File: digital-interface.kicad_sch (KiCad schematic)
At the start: 37 parts, among them U301 Si8641BD-B-IS2, U302 R05C05TE05S

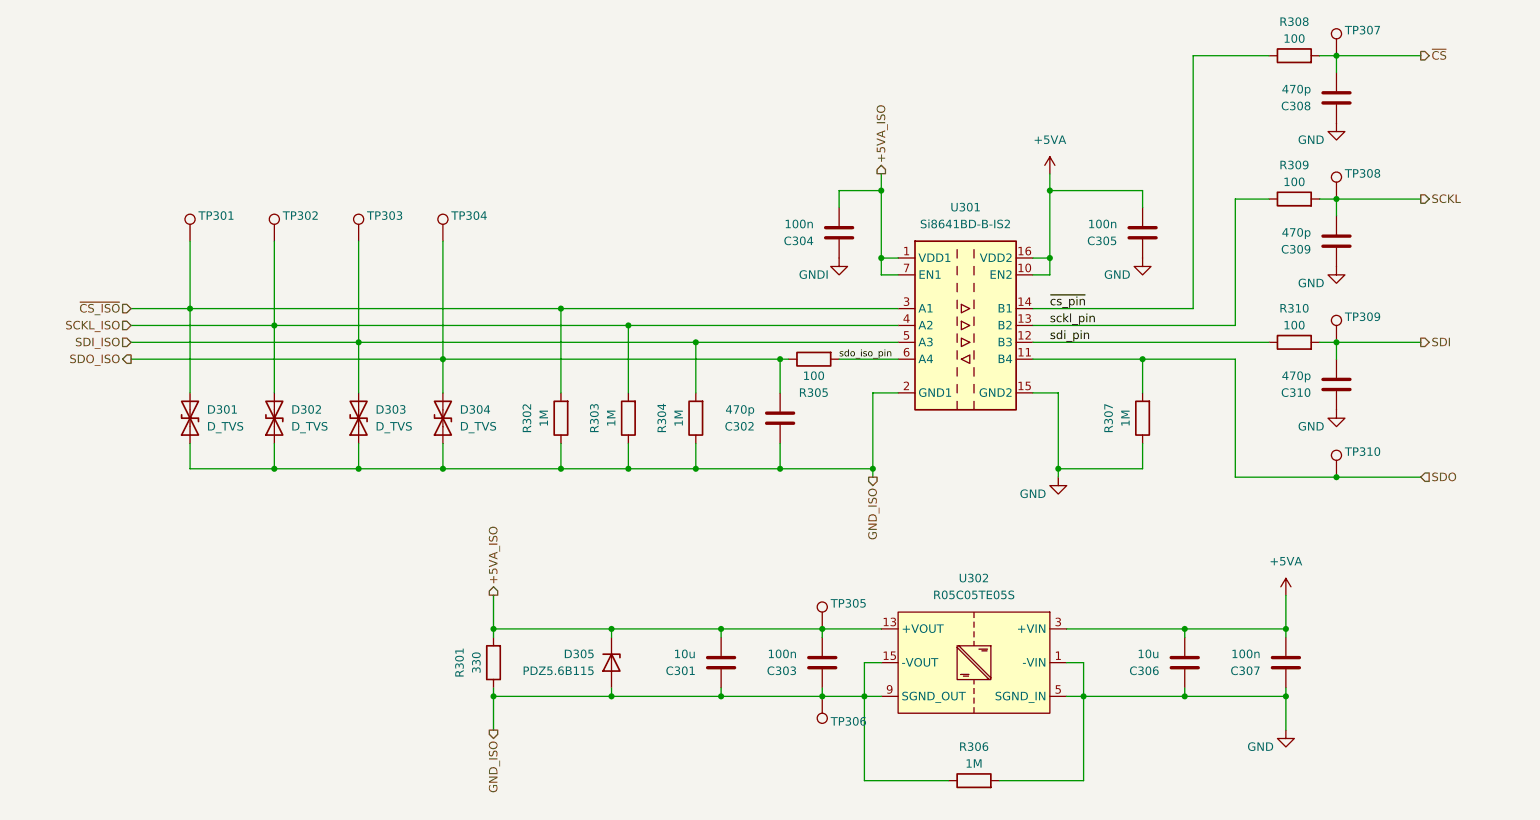
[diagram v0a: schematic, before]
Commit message: fix digital-interface schematic connections
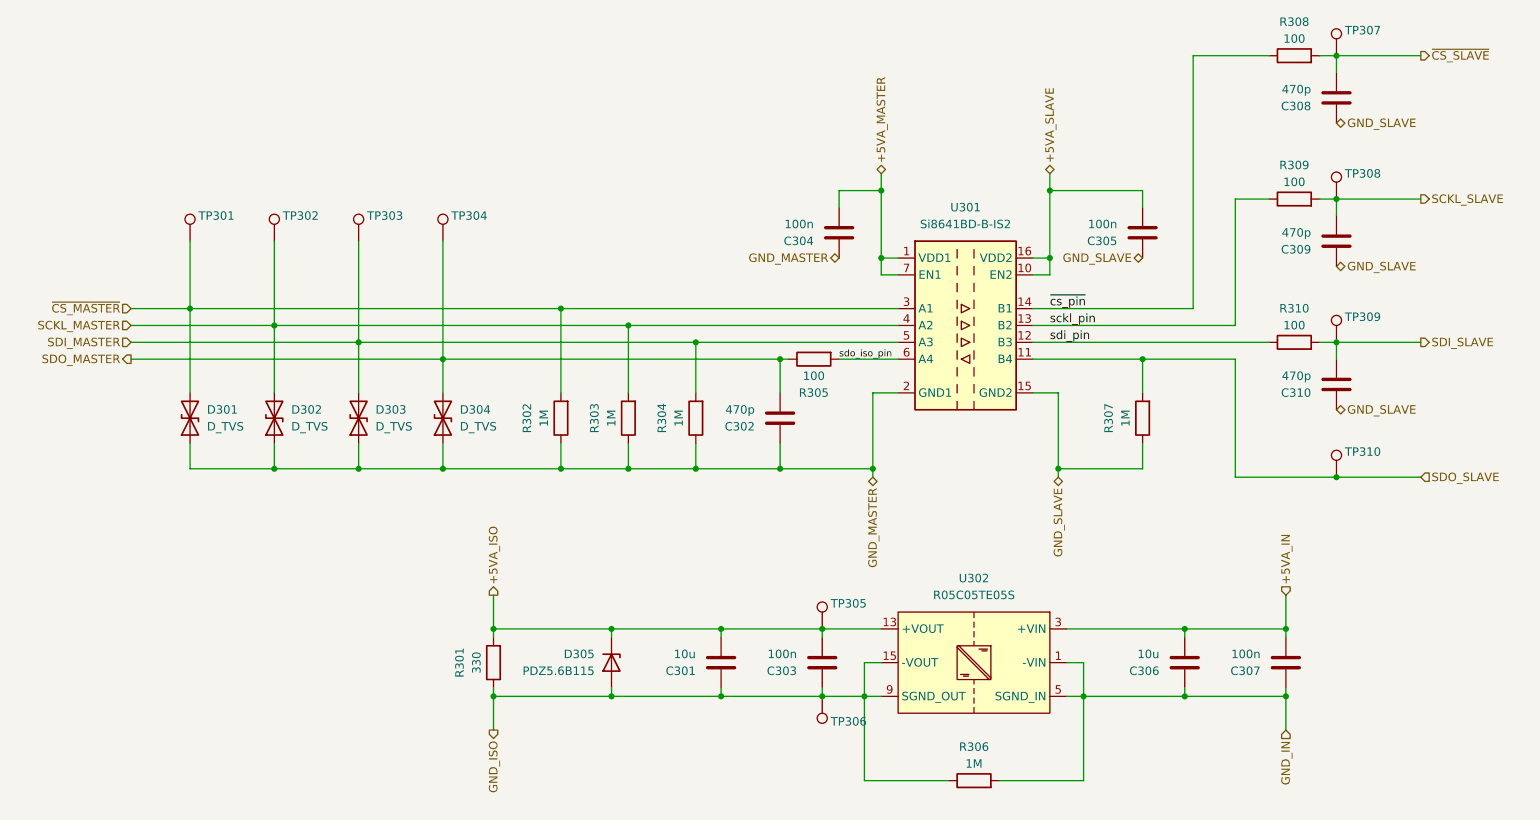
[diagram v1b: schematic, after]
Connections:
- net +5VA_ISO: no longer C304.2, U301.1 (VDD1), U301.7 (EN1)
- net GND_ISO: no longer C302.1, D301.1 (A1), D302.1 (A1), D303.1 (A1), D304.1 (A1), R302.1, R303.1, R304.1, U301.2 (GND1), U301.8 (GND1)
- net +5VA renamed +5VA_IN
- net +5VA_IN: no longer C305.2, U301.10 (EN2), U301.16 (VDD2)
- net GND renamed GND_IN
- net GND_IN: no longer C305.1, C308.1, C309.1, C310.1, R307.1, U301.15 (GND2), U301.9 (GND2)
- net GNDI renamed GND_MASTER
- net GND_MASTER: now also C302.1, D301.1 (A1), D302.1 (A1), D303.1 (A1), D304.1 (A1), R302.1, R303.1, R304.1, U301.2 (GND1), U301.8 (GND1)
- net SCKL renamed SCKL_SLAVE
- net SCKL_ISO renamed SCKL_MASTER
- net SDI renamed SDI_SLAVE
- net SDI_ISO renamed SDI_MASTER
- net SDO renamed SDO_SLAVE
- net SDO_ISO renamed SDO_MASTER
- net ~{CS_ISO} renamed ~{CS_MASTER}
- net ~{CS} renamed ~{CS_SLAVE}
- new net +5VA_MASTER: C304.2, U301.1 (VDD1), U301.7 (EN1)
- new net +5VA_SLAVE: C305.2, U301.10 (EN2), U301.16 (VDD2)
- new net GND_SLAVE: C305.1, C308.1, C309.1, C310.1, R307.1, U301.15 (GND2), U301.9 (GND2)

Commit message: add export of symbol libray, edit symbol links
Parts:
- C301, C302, C303, C304, C305, C306, C307, C308, C309, C310: symbol enclosure:C -> meas:C
- D301, D302, D303, D304: symbol enclosure:D_TVS -> meas:D_TVS
- D305: symbol enclosure:D_Zener -> meas:D_Zener
- R301, R302, R303, R304, R305, R306, R307, R308, R309, R310: symbol enclosure:R -> meas:R
- TP301, TP302, TP303, TP304, TP305, TP306, TP307, TP308, TP309, TP310: symbol enclosure:TestPoint -> meas:TestPoint
- U301: symbol enclosure:Si8641BD-B-IS2 -> meas:Si8641BD-B-IS2
- U302: symbol enclosure:R05C05TE05S -> meas:R05C05TE05S
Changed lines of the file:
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@@
 	)
 	(symbol
-		(lib_id "enclosure:D_TVS")
+		(lib_id "meas:D_TVS")
 		(at 49.53 85.09 90)
 		(unit 1)
@@
 	)
 	(symbol
-		(lib_id "enclosure:D_TVS")
+		(lib_id "meas:D_TVS")
 		(at 62.23 85.09 90)
 		(unit 1)
@@
 	)
 	(symbol
-		(lib_id "enclosure:C")
+		(lib_id "meas:C")
 		(at 222.25 36.83 180)
 		(unit 1)
@@
 	)
 	(symbol
-		(lib_id "enclosure:C")
+		(lib_id "meas:C")
 		(at 214.63 121.92 180)
 		(unit 1)
@@
 	)
 	(symbol
-		(lib_id "enclosure:TestPoint")
+		(lib_id "meas:TestPoint")
 		(at 74.93 58.42 0)
 		(unit 1)
@@
 	)
 	(symbol
-		(lib_id "enclosure:TestPoint")
+		(lib_id "meas:TestPoint")
 		(at 222.25 52.07 0)
 		(unit 1)
@@
 	)
 	(symbol
-		(lib_id "enclosure:C")
+		(lib_id "meas:C")
 		(at 193.04 57.15 180)
 		(unit 1)
@@
 	)
 	(symbol
-		(lib_id "enclosure:TestPoint")
+		(lib_id "meas:TestPoint")
 		(at 49.53 58.42 0)
 		(unit 1)
@@
 	)
 	(symbol
-		(lib_id "enclosure:R")
+		(lib_id "meas:R")
 		(at 143.51 76.2 90)
 		(mirror x)
@@
 	)
 	(symbol
-		(lib_id "enclosure:C")
+		(lib_id "meas:C")
 		(at 199.39 121.92 180)
 		(unit 1)
@@
 	)
 	(symbol
-		(lib_id "enclosure:R")
+		(lib_id "meas:R")
 		(at 167.64 139.7 90)
 		(unit 1)
@@
 	)
 	(symbol
-		(lib_id "enclosure:TestPoint")
+		(lib_id "meas:TestPoint")
 		(at 222.25 93.98 0)
 		(unit 1)
@@
 	)
 	(symbol
-		(lib_id "enclosure:R")
+		(lib_id "meas:R")
 		(at 125.73 85.09 180)
 		(unit 1)
@@
 	)
 	(symbol
-		(lib_id "enclosure:R")
+		(lib_id "meas:R")
 		(at 215.9 30.48 90)
 		(unit 1)
@@
 	)
 	(symbol
-		(lib_id "enclosure:D_Zener")
+		(lib_id "meas:D_Zener")
 		(at 113.03 121.92 270)
 		(unit 1)
@@
 	)
 	(symbol
-		(lib_id "enclosure:C")
+		(lib_id "meas:C")
 		(at 222.25 80.01 180)
 		(unit 1)
@@
 	)
 	(symbol
-		(lib_id "enclosure:R")
+		(lib_id "meas:R")
 		(at 95.25 121.92 180)
 		(unit 1)
@@
 	)
 	(symbol
-		(lib_id "enclosure:TestPoint")
+		(lib_id "meas:TestPoint")
 		(at 87.63 58.42 0)
 		(unit 1)
@@
 	)
 	(symbol
-		(lib_id "enclosure:C")
+		(lib_id "meas:C")
 		(at 222.25 58.42 180)
 		(unit 1)
@@
 	)
 	(symbol
-		(lib_id "enclosure:C")
+		(lib_id "meas:C")
 		(at 129.54 121.92 180)
 		(unit 1)
@@
 	)
 	(symbol
-		(lib_id "enclosure:D_TVS")
+		(lib_id "meas:D_TVS")
 		(at 74.93 85.09 90)
 		(unit 1)
@@
 	)
 	(symbol
-		(lib_id "enclosure:R")
+		(lib_id "meas:R")
 		(at 215.9 52.07 90)
 		(unit 1)
@@
 	)
 	(symbol
-		(lib_id "enclosure:TestPoint")
+		(lib_id "meas:TestPoint")
 		(at 222.25 73.66 0)
 		(unit 1)
@@
 	)
 	(symbol
-		(lib_id "enclosure:R05C05TE05S")
+		(lib_id "meas:R05C05TE05S")
 		(at 167.64 121.92 0)
 		(mirror y)
@@
 	)
 	(symbol
-		(lib_id "enclosure:R")
+		(lib_id "meas:R")
 		(at 215.9 73.66 90)
 		(unit 1)
@@
 	)
 	(symbol
-		(lib_id "enclosure:TestPoint")
+		(lib_id "meas:TestPoint")
 		(at 144.78 116.84 0)
 		(unit 1)
@@
 	)
 	(symbol
-		(lib_id "enclosure:TestPoint")
+		(lib_id "meas:TestPoint")
 		(at 62.23 58.42 0)
 		(unit 1)
@@
 	)
 	(symbol
-		(lib_id "enclosure:C")
+		(lib_id "meas:C")
 		(at 144.78 121.92 180)
 		(unit 1)
@@
 	)
 	(symbol
-		(lib_id "enclosure:TestPoint")
+		(lib_id "meas:TestPoint")
 		(at 222.25 30.48 0)
 		(unit 1)
@@
 	)
 	(symbol
-		(lib_id "enclosure:TestPoint")
+		(lib_id "meas:TestPoint")
 		(at 144.78 127 0)
 		(mirror x)
@@
 	)
 	(symbol
-		(lib_id "enclosure:R")
+		(lib_id "meas:R")
 		(at 105.41 85.09 180)
 		(unit 1)
@@
 	)
 	(symbol
-		(lib_id "enclosure:R")
+		(lib_id "meas:R")
 		(at 115.57 85.09 180)
 		(unit 1)
@@
 	)
 	(symbol
-		(lib_id "enclosure:D_TVS")
+		(lib_id "meas:D_TVS")
 		(at 87.63 85.09 90)
 		(unit 1)
@@
 	)
 	(symbol
-		(lib_id "enclosure:C")
+		(lib_id "meas:C")
 		(at 138.43 85.09 180)
 		(unit 1)
@@
 	)
 	(symbol
-		(lib_id "enclosure:Si8641BD-B-IS2")
+		(lib_id "meas:Si8641BD-B-IS2")
 		(at 166.37 71.12 0)
 		(unit 1)
@@
 	)
 	(symbol
-		(lib_id "enclosure:R")
+		(lib_id "meas:R")
 		(at 193.04 85.09 180)
 		(unit 1)
@@
 	)
 	(symbol
-		(lib_id "enclosure:C")
+		(lib_id "meas:C")
 		(at 147.32 57.15 180)
 		(unit 1)

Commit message: add export of footprint library, edit footprint links
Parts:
- C301, C306: footprint enclosure:C_1210_3225Metric_Pad1.33x2.70mm_HandSolder -> meas:C_1210_3225Metric_Pad1.33x2.70mm_HandSolder
- C302, C303, C304, C305, C307, C308, C309, C310: footprint enclosure:C_0805_2012Metric_Pad1.18x1.45mm_HandSolder -> meas:C_0805_2012Metric_Pad1.18x1.45mm_HandSolder
- D301, D302, D303, D304, D305: footprint enclosure:D_SOD-323_HandSoldering -> meas:D_SOD-323_HandSoldering
- R301, R302, R303, R304, R305, R306, R307, R308, R309, R310: footprint enclosure:R_1210_3225Metric_Pad1.30x2.65mm_HandSolder -> meas:R_1210_3225Metric_Pad1.30x2.65mm_HandSolder
- TP301, TP302, TP303, TP304, TP305, TP306, TP307, TP308, TP309, TP310: footprint enclosure:TP_0805_2012Metric -> meas:TP_0805_2012Metric
- U301, U302: footprint enclosure:SOIC-16W_7.5x10.3mm_P1.27mm -> meas:SOIC-16W_7.5x10.3mm_P1.27mm
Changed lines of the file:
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@@
 			)
 		)
-		(property "Footprint" "enclosure:D_SOD-323_HandSoldering"
+		(property "Footprint" "meas:D_SOD-323_HandSoldering"
 			(at 49.53 85.09 0)
 			(effects
@@
 			)
 		)
-		(property "Footprint" "enclosure:D_SOD-323_HandSoldering"
+		(property "Footprint" "meas:D_SOD-323_HandSoldering"
 			(at 62.23 85.09 0)
 			(effects
@@
 			)
 		)
-		(property "Footprint" "enclosure:C_0805_2012Metric_Pad1.18x1.45mm_HandSolder"
+		(property "Footprint" "meas:C_0805_2012Metric_Pad1.18x1.45mm_HandSolder"
 			(at 221.2848 33.02 0)
 			(effects
@@
 			)
 		)
-		(property "Footprint" "enclosure:C_0805_2012Metric_Pad1.18x1.45mm_HandSolder"
+		(property "Footprint" "meas:C_0805_2012Metric_Pad1.18x1.45mm_HandSolder"
 			(at 213.6648 118.11 0)
 			(effects
@@
 			)
 		)
-		(property "Footprint" "enclosure:TP_0805_2012Metric"
+		(property "Footprint" "meas:TP_0805_2012Metric"
 			(at 80.01 58.42 0)
 			(effects
@@
 			)
 		)
-		(property "Footprint" "enclosure:TP_0805_2012Metric"
+		(property "Footprint" "meas:TP_0805_2012Metric"
 			(at 227.33 52.07 0)
 			(effects
@@
 			)
 		)
-		(property "Footprint" "enclosure:C_0805_2012Metric_Pad1.18x1.45mm_HandSolder"
+		(property "Footprint" "meas:C_0805_2012Metric_Pad1.18x1.45mm_HandSolder"
 			(at 192.0748 53.34 0)
 			(effects
@@
 			)
 		)
-		(property "Footprint" "enclosure:TP_0805_2012Metric"
+		(property "Footprint" "meas:TP_0805_2012Metric"
 			(at 54.61 58.42 0)
 			(effects
@@
 			)
 		)
-		(property "Footprint" "enclosure:R_1210_3225Metric_Pad1.30x2.65mm_HandSolder"
+		(property "Footprint" "meas:R_1210_3225Metric_Pad1.30x2.65mm_HandSolder"
 			(at 143.51 74.422 90)
 			(effects
@@
 			)
 		)
-		(property "Footprint" "enclosure:C_1210_3225Metric_Pad1.33x2.70mm_HandSolder"
+		(property "Footprint" "meas:C_1210_3225Metric_Pad1.33x2.70mm_HandSolder"
 			(at 198.4248 118.11 0)
 			(effects
@@
 			)
 		)
-		(property "Footprint" "enclosure:R_1210_3225Metric_Pad1.30x2.65mm_HandSolder"
+		(property "Footprint" "meas:R_1210_3225Metric_Pad1.30x2.65mm_HandSolder"
 			(at 167.64 141.478 90)
 			(effects
@@
 			)
 		)
-		(property "Footprint" "enclosure:TP_0805_2012Metric"
+		(property "Footprint" "meas:TP_0805_2012Metric"
 			(at 227.33 93.98 0)
 			(effects
@@
 			)
 		)
-		(property "Footprint" "enclosure:R_1210_3225Metric_Pad1.30x2.65mm_HandSolder"
+		(property "Footprint" "meas:R_1210_3225Metric_Pad1.30x2.65mm_HandSolder"
 			(at 127.508 85.09 90)
 			(effects
@@
 			)
 		)
-		(property "Footprint" "enclosure:R_1210_3225Metric_Pad1.30x2.65mm_HandSolder"
+		(property "Footprint" "meas:R_1210_3225Metric_Pad1.30x2.65mm_HandSolder"
 			(at 215.9 32.258 90)
 			(effects
@@
 			)
 		)
-		(property "Footprint" "enclosure:D_SOD-323_HandSoldering"
+		(property "Footprint" "meas:D_SOD-323_HandSoldering"
 			(at 113.03 121.92 0)
 			(effects
@@
 			)
 		)
-		(property "Footprint" "enclosure:C_0805_2012Metric_Pad1.18x1.45mm_HandSolder"
+		(property "Footprint" "meas:C_0805_2012Metric_Pad1.18x1.45mm_HandSolder"
 			(at 221.2848 76.2 0)
 			(effects
@@
 			)
 		)
-		(property "Footprint" "enclosure:R_1210_3225Metric_Pad1.30x2.65mm_HandSolder"
+		(property "Footprint" "meas:R_1210_3225Metric_Pad1.30x2.65mm_HandSolder"
 			(at 97.028 121.92 90)
 			(effects
@@
 			)
 		)
-		(property "Footprint" "enclosure:TP_0805_2012Metric"
+		(property "Footprint" "meas:TP_0805_2012Metric"
 			(at 92.71 58.42 0)
 			(effects
@@
 			)
 		)
-		(property "Footprint" "enclosure:C_0805_2012Metric_Pad1.18x1.45mm_HandSolder"
+		(property "Footprint" "meas:C_0805_2012Metric_Pad1.18x1.45mm_HandSolder"
 			(at 221.2848 54.61 0)
 			(effects
@@
 			)
 		)
-		(property "Footprint" "enclosure:C_1210_3225Metric_Pad1.33x2.70mm_HandSolder"
+		(property "Footprint" "meas:C_1210_3225Metric_Pad1.33x2.70mm_HandSolder"
 			(at 128.5748 118.11 0)
 			(effects
@@
 			)
 		)
-		(property "Footprint" "enclosure:D_SOD-323_HandSoldering"
+		(property "Footprint" "meas:D_SOD-323_HandSoldering"
 			(at 74.93 85.09 0)
 			(effects
@@
 			)
 		)
-		(property "Footprint" "enclosure:R_1210_3225Metric_Pad1.30x2.65mm_HandSolder"
+		(property "Footprint" "meas:R_1210_3225Metric_Pad1.30x2.65mm_HandSolder"
 			(at 215.9 53.848 90)
 			(effects
@@
 			)
 		)
-		(property "Footprint" "enclosure:TP_0805_2012Metric"
+		(property "Footprint" "meas:TP_0805_2012Metric"
 			(at 227.33 73.66 0)
 			(effects
@@
 			)
 		)
-		(property "Footprint" "enclosure:SOIC-16W_7.5x10.3mm_P1.27mm"
+		(property "Footprint" "meas:SOIC-16W_7.5x10.3mm_P1.27mm"
 			(at 167.64 121.92 0)
 			(effects
@@
 			)
 		)
-		(property "Footprint" "enclosure:R_1210_3225Metric_Pad1.30x2.65mm_HandSolder"
+		(property "Footprint" "meas:R_1210_3225Metric_Pad1.30x2.65mm_HandSolder"
 			(at 215.9 75.438 90)
 			(effects
@@
 			)
 		)
-		(property "Footprint" "enclosure:TP_0805_2012Metric"
+		(property "Footprint" "meas:TP_0805_2012Metric"
 			(at 149.86 116.84 0)
 			(effects
@@
 			)
 		)
-		(property "Footprint" "enclosure:TP_0805_2012Metric"
+		(property "Footprint" "meas:TP_0805_2012Metric"
 			(at 67.31 58.42 0)
 			(effects
@@
 			)
 		)
-		(property "Footprint" "enclosure:C_0805_2012Metric_Pad1.18x1.45mm_HandSolder"
+		(property "Footprint" "meas:C_0805_2012Metric_Pad1.18x1.45mm_HandSolder"
 			(at 143.8148 118.11 0)
 			(effects
@@
 			)
 		)
-		(property "Footprint" "enclosure:TP_0805_2012Metric"
+		(property "Footprint" "meas:TP_0805_2012Metric"
 			(at 227.33 30.48 0)
 			(effects
@@
 			)
 		)
-		(property "Footprint" "enclosure:TP_0805_2012Metric"
+		(property "Footprint" "meas:TP_0805_2012Metric"
 			(at 149.86 127 0)
 			(effects
@@
 			)
 		)
-		(property "Footprint" "enclosure:R_1210_3225Metric_Pad1.30x2.65mm_HandSolder"
+		(property "Footprint" "meas:R_1210_3225Metric_Pad1.30x2.65mm_HandSolder"
 			(at 107.188 85.09 90)
 			(effects
@@
 			)
 		)
-		(property "Footprint" "enclosure:R_1210_3225Metric_Pad1.30x2.65mm_HandSolder"
+		(property "Footprint" "meas:R_1210_3225Metric_Pad1.30x2.65mm_HandSolder"
 			(at 117.348 85.09 90)
 			(effects
@@
 			)
 		)
-		(property "Footprint" "enclosure:D_SOD-323_HandSoldering"
+		(property "Footprint" "meas:D_SOD-323_HandSoldering"
 			(at 87.63 85.09 0)
 			(effects
@@
 			)
 		)
-		(property "Footprint" "enclosure:C_0805_2012Metric_Pad1.18x1.45mm_HandSolder"
+		(property "Footprint" "meas:C_0805_2012Metric_Pad1.18x1.45mm_HandSolder"
 			(at 137.4648 81.28 0)
 			(effects
@@
 			)
 		)
-		(property "Footprint" "enclosure:SOIC-16W_7.5x10.3mm_P1.27mm"
+		(property "Footprint" "meas:SOIC-16W_7.5x10.3mm_P1.27mm"
 			(at 166.37 85.09 0)
 			(effects
@@
 			)
 		)
-		(property "Footprint" "enclosure:R_1210_3225Metric_Pad1.30x2.65mm_HandSolder"
+		(property "Footprint" "meas:R_1210_3225Metric_Pad1.30x2.65mm_HandSolder"
 			(at 194.818 85.09 90)
 			(effects
@@
 			)
 		)
-		(property "Footprint" "enclosure:C_0805_2012Metric_Pad1.18x1.45mm_HandSolder"
+		(property "Footprint" "meas:C_0805_2012Metric_Pad1.18x1.45mm_HandSolder"
 			(at 146.3548 53.34 0)
 			(effects
